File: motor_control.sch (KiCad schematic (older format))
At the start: 15 parts, among them J5 Motor1, J6 Motor2, J7 Motor3, J8 Motor4, U6 DRV8833PW, U7 DRV8833PW

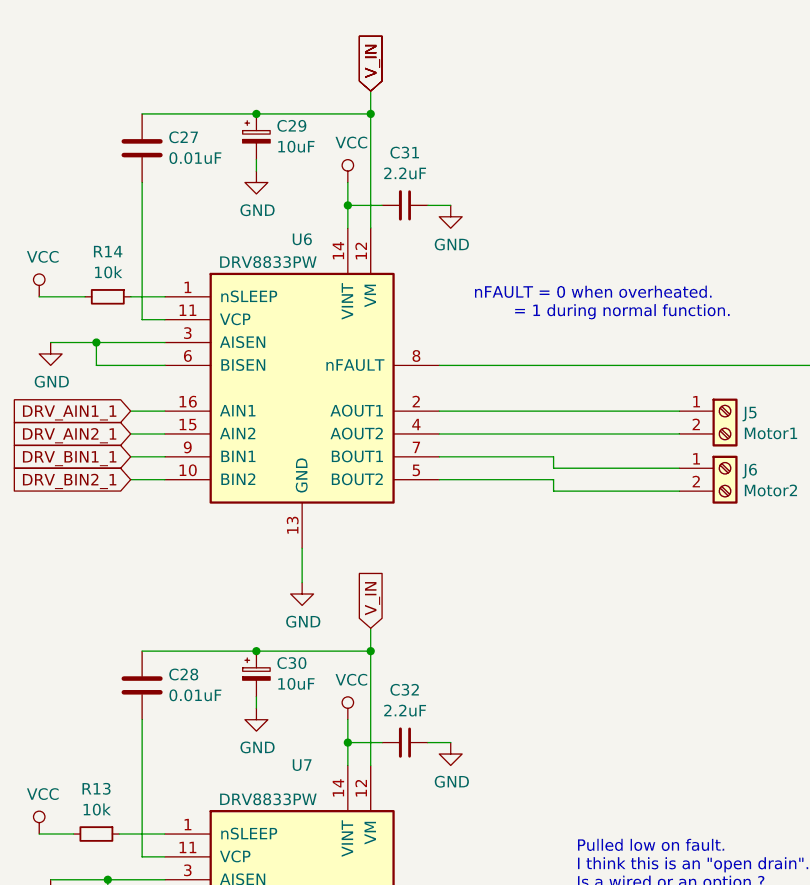
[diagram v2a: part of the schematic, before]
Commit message: adding an nrf52
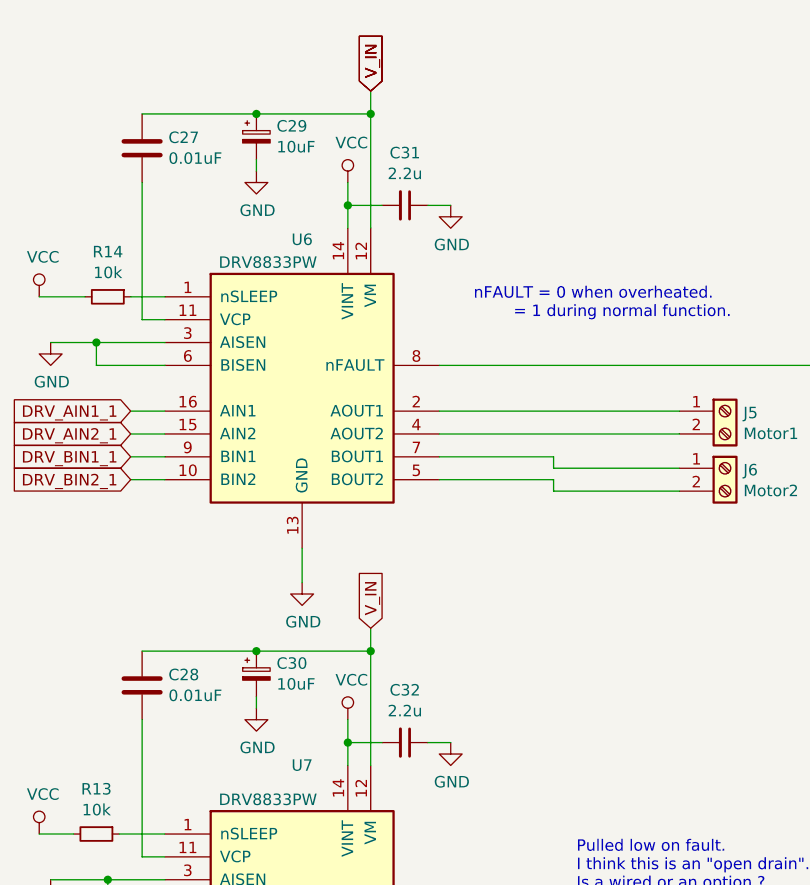
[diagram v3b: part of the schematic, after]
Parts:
- C31, C32: value 2.2uF -> 2.2u
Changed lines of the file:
@@
 $Descr A4 11693 8268
 encoding utf-8
-Sheet 5 5
+Sheet 5 6
 Title ""
 Date ""
@@
 P 6000 1450
 F 0 "C31" V 5771 1450 50  0000 C CNN
-F 1 "2.2uF" V 5862 1450 50  0000 C CNN
+F 1 "2.2u" V 5862 1450 50  0000 C CNN
 F 2 "Capacitor_SMD:C_0603_1608Metric" H 6000 1450 50  0001 C CNN
 F 3 "~" H 6000 1450 50  0001 C CNN
@@
 P 6000 3800
 F 0 "C32" V 5771 3800 50  0000 C CNN
-F 1 "2.2uF" V 5862 3800 50  0000 C CNN
+F 1 "2.2u" V 5862 3800 50  0000 C CNN
 F 2 "Capacitor_SMD:C_0603_1608Metric" H 6000 3800 50  0001 C CNN
 F 3 "~" H 6000 3800 50  0001 C CNN
